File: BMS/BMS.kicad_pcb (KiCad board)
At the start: 4 copper layers, 151.1 x 100 mm, 323 parts, among them IC1 STM32H742VIT6, IC2 TPS563200DDCR, J1 Conn_01x17, J10 Conn_01x06, J11 Conn_01x06, J12 Conn_01x17, J13 USB_A, J14 USB_C_Receptacle_USB2.0_14P, J15 Harwin M80-8542042, J16 Harwin M80-8542042, J17 Conn_01x04, J18 Conn_01x02, J7 FTSH-107-01-L-D-K, J8 Conn_01x02, J9 Conn_01x06, Q1 NPN, Q2 NPN, Q3 DMT6018LDR-7, Q4 DMT6018LDR-7, Q5 DMT6018LDR-7, Q6 DMT6018LDR-7, SW1 SW_Push, U1 BQ79614PAPRQ1, U2 BQ79614PAPRQ1, U3 PBQ79600PWQ1, U4 MCP2542FD-E/MF, U5 PTPSM863253RDXR

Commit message: zmiany w bq79614 layout
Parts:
- added TH1: 10k b= 3000, Resistor_SMD:R_0603_1608Metric_Pad0.98x0.95mm_HandSolder, F.Cu at (112.2, 55.6)
- J16: value Harwin M80-8542042 -> Conn_01x10; footprint footrpint:HARWIN_M80-8542042 -> footrpint:HARWIN_G125-MV11005L1P
- moved C59 249.7 mm to (140.6, 73.2), turned to -90 degrees
- moved C60 248.2 mm to (145.7, 73.2), turned to -90 degrees
- moved C62 247.5 mm to (144.2, 69.9), turned to -90 degrees
- moved C61 245.1 mm to (142.1, 69.9), turned to -90 degrees
- moved R67 242.1 mm to (143.2, 75.7)
- moved R68 241.5 mm to (142.1, 73.2), turned to 90 degrees
- moved R71 99.9 mm to (144.2, 73.2), turned to 90 degrees
- moved J18 81.3 mm to (200.1, -20.4)
- moved R165 81.3 mm to (194.9, -24.5)
- moved U5 81.3 mm to (189.9, -12.2)
- moved C119 81.3 mm to (181.3, -22.4)
- moved C120 81.3 mm to (178.6, -22.6)
- moved C121 81.3 mm to (190.7, -24.8)
- moved C122 81.3 mm to (177.2, -25.2)
- moved C123 81.3 mm to (177.2, -27.4)
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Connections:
- C9 pad 1: Net-(U1-AVSS) -> Stack-
- J1 pad 1: Stack- -> unconnected-(J1-Pin_1-Pad1)
- J1 pad 14: Batt_Coupling -> Net-(J1-Pin_14)
- J1 pad 15: unconnected-(J1-Pin_15-Pad15) -> Net-(J1-Pin_15)
- J1 pad 16: unconnected-(J1-Pin_16-Pad16) -> Net-(J1-Pin_16)
- J1 pad 17: unconnected-(J1-Pin_17-Pad17) -> Batt_Coupling
- J1 pad 2: Net-(J1-Pin_2) -> unconnected-(J1-Pin_2-Pad2)
- J1 pad 3: Net-(J1-Pin_3) -> unconnected-(J1-Pin_3-Pad3)
- J1 pad 4: Net-(J1-Pin_4) -> Stack-
- J16 pad 1: Stack- -> /Mesurements_LTC1/Temperature_LTC_1/Thermistor2
- J16 pad 10: unconnected-(J16-Pad10) -> /Mesurements_LTC1/Temperature_LTC_1/Thermistor7
- J16 pad 2: Stack- -> /Mesurements_LTC1/Temperature_LTC_1/Thermistor3
- J16 pad 3: Stack- -> /Mesurements_LTC1/Temperature_LTC_1/Thermistor4
- J16 pad 4: Stack- -> /Mesurements_LTC1/Temperature_LTC_1/Thermistor5
- J16 pad 5: Stack- -> /Mesurements_LTC1/Temperature_LTC_1/Thermistor6
- J16 pad 9: unconnected-(J16-Pad9) -> /Mesurements_LTC1/Temperature_LTC_1/Thermistor8
- R14 pad 2: /Mesurements_LTC1/Temperature_LTC_1/Thermistor1 -> Net-(R14-Pad2)
- R15 pad 1: /Mesurements_LTC1/Temperature_LTC_1/Thermistor1 -> Net-(R14-Pad2)
- R21 pad 1: Net-(J1-Pin_13) -> Net-(J1-Pin_16)
- R22 pad 1: Net-(J1-Pin_12) -> Net-(J1-Pin_15)
- R23 pad 1: Net-(J1-Pin_11) -> Net-(J1-Pin_14)
- R24 pad 1: Net-(J1-Pin_10) -> Net-(J1-Pin_13)
- R25 pad 1: Net-(J1-Pin_9) -> Net-(J1-Pin_12)
- R26 pad 1: Net-(J1-Pin_8) -> Net-(J1-Pin_11)
- R27 pad 1: Net-(J1-Pin_7) -> Net-(J1-Pin_10)
- R28 pad 1: Net-(J1-Pin_6) -> Net-(J1-Pin_9)
- R29 pad 1: Net-(J1-Pin_5) -> Net-(J1-Pin_8)
- R30 pad 1: Net-(J1-Pin_4) -> Net-(J1-Pin_7)
- R31 pad 1: Net-(J1-Pin_3) -> Net-(J1-Pin_6)
- R32 pad 1: Net-(J1-Pin_2) -> Net-(J1-Pin_5)
- R34 pad 1: Net-(J1-Pin_13) -> Net-(J1-Pin_16)
- R35 pad 1: Net-(J1-Pin_12) -> Net-(J1-Pin_15)
- R36 pad 1: Net-(J1-Pin_11) -> Net-(J1-Pin_14)
- R37 pad 1: Net-(J1-Pin_10) -> Net-(J1-Pin_13)
- R38 pad 1: Net-(J1-Pin_9) -> Net-(J1-Pin_12)
- R39 pad 1: Net-(J1-Pin_8) -> Net-(J1-Pin_11)
- R40 pad 1: Net-(J1-Pin_7) -> Net-(J1-Pin_10)
- R41 pad 1: Net-(J1-Pin_6) -> Net-(J1-Pin_9)
- R42 pad 1: Net-(J1-Pin_5) -> Net-(J1-Pin_8)
- R43 pad 1: Net-(J1-Pin_4) -> Net-(J1-Pin_7)
- R44 pad 1: Net-(J1-Pin_3) -> Net-(J1-Pin_6)
- R45 pad 1: Net-(J1-Pin_2) -> Net-(J1-Pin_5)
- R8 pad 2: /Mesurements_LTC1/Temperature_LTC_1/Thermistor1 -> Net-(R14-Pad2)
- U1 pad 39: Net-(U1-AVSS) -> Stack-
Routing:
- net Stack-: track 7.50 -> 99.6 mm, vias 0 -> 68
- net Net-(J1-Pin_13): track 96.3 -> 26.5 mm, vias 1 -> 0
- net Net-(J1-Pin_12): track 92.9 -> 29.0 mm, vias 1 -> 0
- net Net-(J1-Pin_11): track 87.9 -> 31.9 mm, vias 1 -> 0
- net Net-(J1-Pin_10): track 83.7 -> 34.6 mm, vias 1 -> 0
- net /Mesurements_LTC1/VC7: track 84.7 -> 39.8 mm
- net Net-(J1-Pin_9): track 76.7 -> 38.0 mm, vias 1 -> 0
- net /Mesurements_LTC1/CB13: track 27.5 -> 58.4 mm, vias 0 -> 2
- net /Mesurements_LTC1/CB0: track 19.2 -> 49.8 mm, vias 0 -> 2
- net Net-(J1-Pin_5): track 19.7 -> 48.4 mm, vias 1 -> 0
- net /Mesurements_LTC1/CB1: track 17.5 -> 44.0 mm, vias 0 -> 2
- net /Mesurements_LTC1/CB2: track 15.7 -> 40.7 mm, vias 0 -> 2
- net /Mesurements_LTC1/CB12: track 31.3 -> 55.9 mm, vias 0 -> 2
- net Net-(J1-Pin_6): track 22.2 -> 45.7 mm, vias 1 -> 0
- net Net-(J1-Pin_14): track 0.00 -> 23.0 mm
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- added copper zone on F.Cu, net Stack-
- added copper zone on In1.Cu, net Stack-
- added copper zone on In2.Cu, net Stack-
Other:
- board size 151.1 x 100 mm -> 129.9 x 93.1 mm

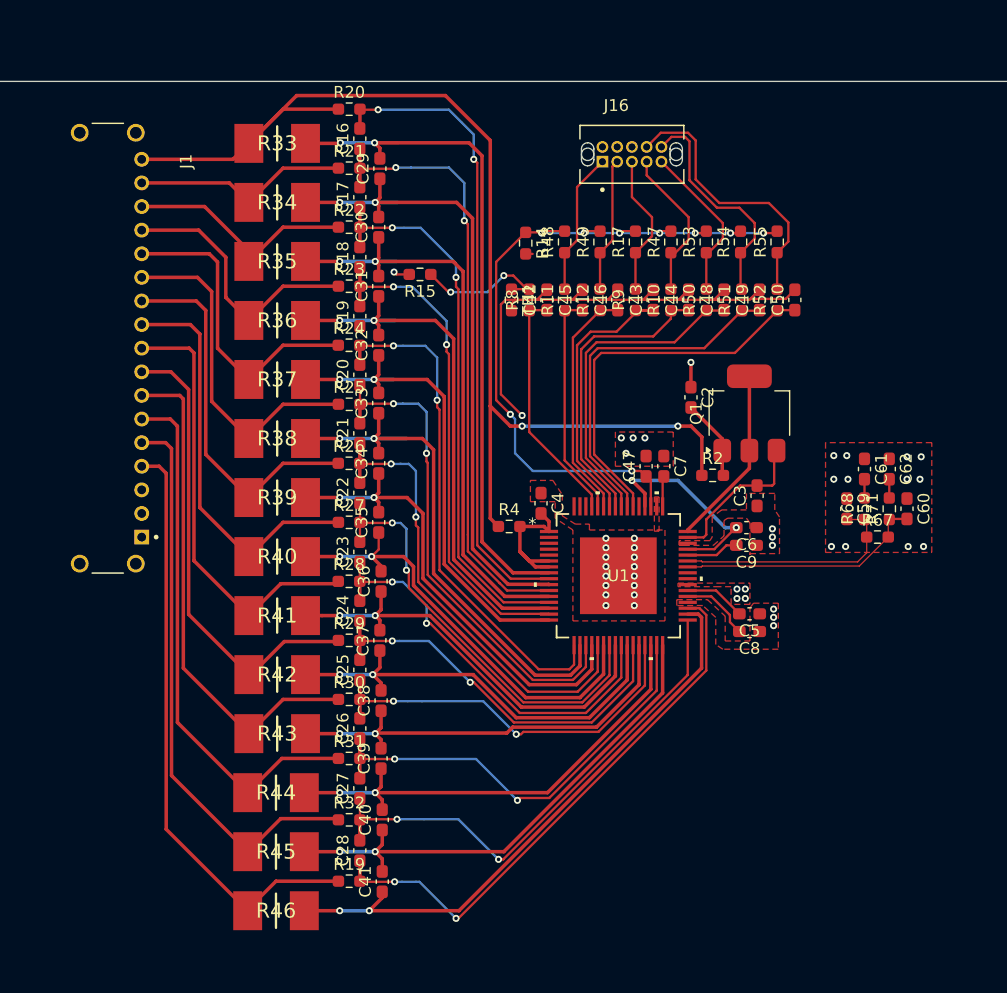
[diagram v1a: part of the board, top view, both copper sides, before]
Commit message: zmiana polozenia zlacza oraz ukladu bq, jak i zmiena via na thru
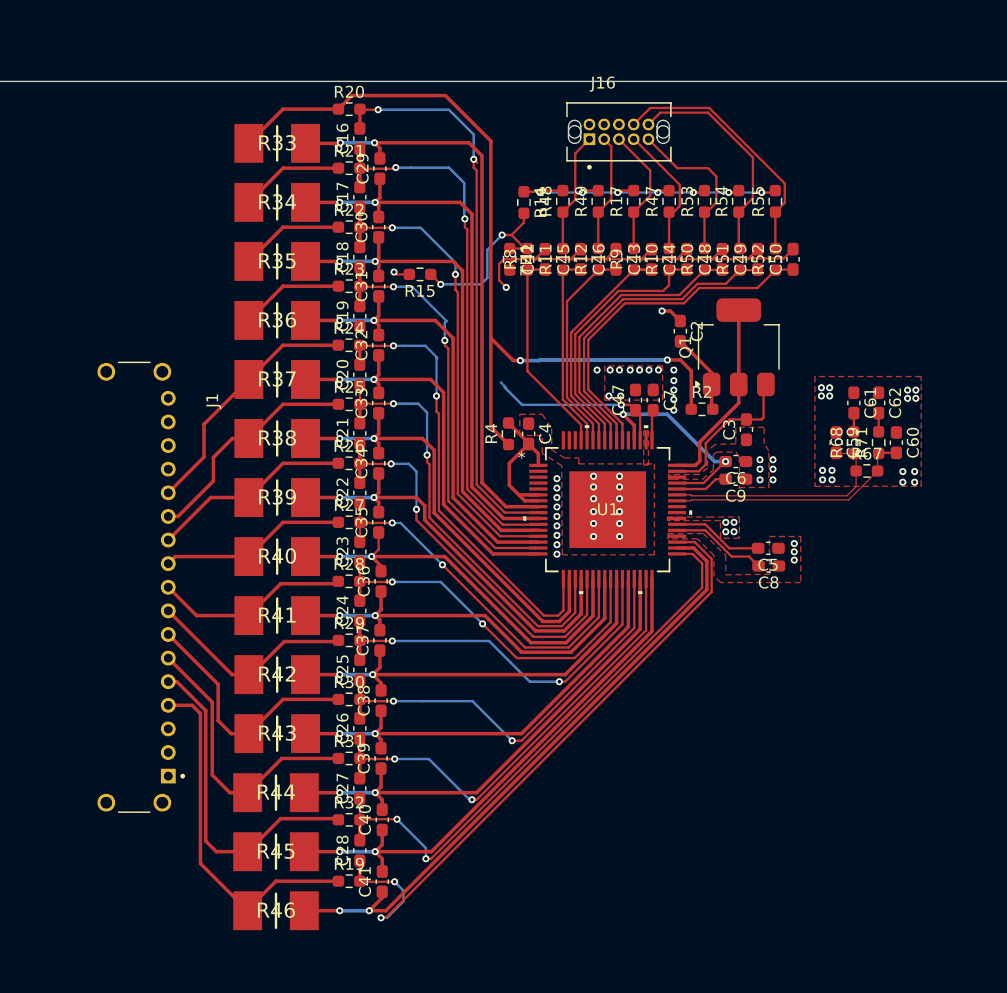
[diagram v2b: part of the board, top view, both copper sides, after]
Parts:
- moved J1 20.4 mm to (80.2, 79.9)
- moved R4 7.85 mm to (111.9, 66.9), turned to 90 degrees
- moved C4 5.98 mm to (113.6, 66.9)
- moved C8 5.78 mm to (133.9, 78.1)
- moved C5 5.77 mm to (133.9, 76.6)
- moved C61 5.67 mm to (141.2, 64.3)
- moved C62 5.67 mm to (143.2, 64.3)
- moved R2 5.67 mm to (128.3, 64.8)
- moved R67 5.67 mm to (142.2, 70.0)
- moved C47 5.67 mm to (122.7, 64.0)
- moved C7 5.67 mm to (124.2, 64.0)
- moved U1 5.67 mm to (120.3, 73.3)
- moved C3 5.67 mm to (132.1, 66.5)
- moved Q1 5.67 mm to (131.4, 59.6)
- moved C2 5.67 mm to (126.5, 58.2)
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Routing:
- net Stack-: track 99.6 -> 70.6 mm, vias 68 -> 67
- net Batt_Coupling: track 97.4 -> 71.5 mm
- net Net-(J1-Pin_7): track 43.1 -> 20.9 mm
- net Net-(J1-Pin_8): track 39.6 -> 17.9 mm
- net Net-(J1-Pin_6): track 45.7 -> 24.0 mm
- net Net-(J1-Pin_9): track 38.0 -> 17.0 mm
- net Net-(J1-Pin_5): track 48.4 -> 28.1 mm
- net /Mesurements_LTC1/Temperature_LTC_1/TSREF: track 64.2 -> 44.4 mm, vias 9 -> 8
- net Net-(J1-Pin_10): track 34.6 -> 16.1 mm
- net Net-(J1-Pin_11): track 31.9 -> 17.1 mm
- net Net-(J1-Pin_14): track 23.0 -> 8.79 mm
- net Net-(J1-Pin_15): track 20.4 -> 8.86 mm
- net Net-(J1-Pin_16): track 18.5 -> 8.79 mm
- net Net-(J1-Pin_12): track 29.0 -> 19.5 mm
- net /Mesurements_LTC1/CB13: track 58.4 -> 50.3 mm
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
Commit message: Dodano layout drugiego bq79614, ukladu tlumaczącego z protokułu TI na UART oraz wstępnie poprowadzono pary różnicowe
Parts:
- removed F2: 1 ALBO 2 A, Resistor_SMD:R_0402_1005Metric_Pad0.72x0.64mm_HandSolder
- removed J11, J9: Conn_01x06, footrpint:HARWIN_M300-MV30645M1
- removed J15: Harwin M80-8542042, footrpint:HARWIN_M80-8542042
- removed J17: Conn_01x04, footrpint:HARWIN_M80-5100442
- removed J18: Conn_01x02, footrpint:HARWIN_M80-5000000M1-02-PM1-00-000
- removed J5, J6: ~, footrpint:HARWIN_M80-5000000M1-02-PM1-00-000
- removed J8: Conn_01x02, footrpint:HARWIN_M55-3100242R
- removed Q5: DMT6018LDR-7, Samacsys:DMT6018LDR7
- removed R162: 100, Resistor_SMD:R_0603_1608Metric
- removed R164: 4.7k, Resistor_SMD:R_0603_1608Metric
- added J19: Conn_02x13_Counter_Clockwise, footrpint:HARWIN_M80-5402642, F.Cu at (-16.5, 173.1)
- added TH13: 10k b= 3000, Resistor_SMD:R_0603_1608Metric_Pad0.98x0.95mm_HandSolder, F.Cu at (111.5, 127.5)
- J10: value Conn_01x06 -> Conn_01x10; footprint footrpint:HARWIN_M300-MV30645M1 -> footrpint:HARWIN_G125-MV11005L1P
- moved J10 259.2 mm to (121.5, 117.6)
- moved C64 259.0 mm to (149.2, 164.1), turned to -90 degrees
- moved C63 254.9 mm to (144.3, 164.1), turned to -90 degrees
- moved R74 251.2 mm to (146.8, 166.5)
- moved R73 250.3 mm to (145.8, 164.1), turned to -90 degrees
- moved C54 245.9 mm to (133.8, 151.2), turned to 180 degrees
- moved C57 244.7 mm to (133.8, 152.8), turned to 180 degrees
- moved C52 243.4 mm to (132.4, 141.0), turned to 90 degrees
- moved C55 241.4 mm to (131.2, 144.3), turned to 180 degrees
- moved C58 240.4 mm to (131.2, 145.8), turned to 180 degrees
- moved U3 235.5 mm to (148.0, 175.2), turned to 180 degrees
- moved C51 234.5 mm to (124.1, 134.4), turned to 90 degrees
- moved C56 233.0 mm to (124.1, 138.0), turned to -90 degrees
- moved R64 228.6 mm to (126.7, 140.0)
- moved C53 224.7 mm to (113.6, 142.0), turned to -90 degrees
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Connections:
- net Net-(C12-Pad1) renamed /galvanic_isulation_2/S2+
- net Net-(C12-Pad2) renamed /galvanic_isulation_2/S1+
- net Net-(C13-Pad1) renamed /galvanic_isulation_2/S2-
- net Net-(C13-Pad2) renamed /galvanic_isulation_2/S1-
- net Net-(C130-Pad1) renamed /galvanic_isulation_1/S2+
- net Net-(C130-Pad2) renamed /galvanic_isulation_1/S1+
- net Net-(C131-Pad1) renamed /galvanic_isulation_1/S2-
- net Net-(C131-Pad2) renamed /galvanic_isulation_1/S1-
- net Net-(C61-Pad1) renamed /galvanic_isulation_0/S2+
- net Net-(C61-Pad2) renamed /galvanic_isulation_0/S1+
- net Net-(C62-Pad1) renamed /galvanic_isulation_0/S2-
- net Net-(C62-Pad2) renamed /galvanic_isulation_0/S1-
- net Net-(D1-A) renamed /Connectivity/Relay_OUT
- net Net-(D13-A) renamed /Connectivity/PreCharge_OUT
- C115 pad 2: +5V -> /Connectivity/+5V_curr_sense
- C122 pad 1: /Power/5V/+5V_OUT -> +5V
- C123 pad 1: /Power/5V/+5V_OUT -> +5V
- C126 pad 1: /Power/5V/+5V_OUT -> +5V
- C127 pad 1: /Power/5V/+5V_OUT -> +5V
- D6 pad 1: +5V -> /Connectivity/+5V_curr_sense
- D8 pad 2: Net-(D8-A) -> VBUS
- F1 pad 2: /Connectivity/Ext_5V -> /Connectivity/5V_fused
- IC1 pad 30: /3.3V_Enable -> unconnected-(IC1-PA6-Pad30)
- J10 pad 1: /Connectivity/Ext_3.3V -> /Mesurements_LTC2/Temperature_LTC_2/Thermistor2
- J10 pad 2: Net-(J10-Pin_2) -> /Mesurements_LTC2/Temperature_LTC_2/Thermistor3
- J10 pad 3: /Connectivity/Ext_3.3V -> /Mesurements_LTC2/Temperature_LTC_2/Thermistor4
- J10 pad 4: Net-(J10-Pin_2) -> /Mesurements_LTC2/Temperature_LTC_2/Thermistor5
- J10 pad 5: /Connectivity/Ext_3.3V -> /Mesurements_LTC2/Temperature_LTC_2/Thermistor6
- J10 pad 6: Net-(J10-Pin_2) -> Batt_Coupling
- J13 pad 1: Net-(J13-VBUS) -> VBUS
- L1 pad 2: /Power/5V/+5V_OUT -> +5V
- Q4 pad 6: Net-(J9-Pin_2) -> /Connectivity/5V_fused_minus
- R149 pad 1: /Connectivity/B1_IN -> /Connectivity/B2_IN
- R156 pad 1: /Connectivity/B2_IN -> /Connectivity/B3_IN
- R158 pad 1: /Connectivity/B3_IN -> /Connectivity/B4_IN
- R165 pad 2: /Power/5V/+5V_OUT -> +5V
- R61 pad 1: /Power/5V/+5V_OUT -> +5V
- U5 pad 1: /Power/5V/+5V_OUT -> +5V
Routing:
- net Batt_Coupling: track 71.5 -> 270.6 mm, vias 2 -> 78
- net CELL26: track 0.00 -> 81.0 mm, vias 0 -> 2
- net +5V: track 0.00 -> 60.5 mm
- net /Power/5V/+5V_OUT: track 60.5 -> 0.00 mm
- net /galvanic_isulation_0/S2-: track 0.00 -> 53.5 mm, vias 0 -> 2
- net /Mesurements_LTC2/CB0: track 0.00 -> 52.8 mm, vias 0 -> 2
- net /galvanic_isulation_0/S2+: track 0.00 -> 52.6 mm
- net /Mesurements_LTC2/CB13: track 0.00 -> 50.2 mm, vias 0 -> 2
- net /Mesurements_LTC2/VC0: track 0.00 -> 49.7 mm, vias 0 -> 2
- net /Mesurements_LTC2/VC1: track 0.00 -> 48.2 mm, vias 0 -> 2
- net /Mesurements_LTC2/CB12: track 0.00 -> 47.8 mm, vias 0 -> 2
- net /Mesurements_LTC2/VC13: track 0.00 -> 46.6 mm, vias 0 -> 2
- net /galvanic_isulation_0/S1+: track 1.59 -> 47.5 mm
- net /Mesurements_LTC2/CB1: track 0.00 -> 45.6 mm, vias 0 -> 2
- net /galvanic_isulation_0/S1-: track 1.59 -> 46.7 mm
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- added copper zone on F.Cu, net Batt_Coupling
- added copper zone on In1.Cu, net Batt_Coupling
- added copper zone on In2.Cu, net Batt_Coupling
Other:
- board size 129.9 x 93.1 mm -> 119.4 x 147.2 mm

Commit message: Iteracja 1.0 gotowa, teraz sprawdzenie i zmiany kosmetyczne
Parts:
- removed J14: USB_C_Receptacle_USB2.0_14P, Connector_USB:USB_C_Receptacle_GCT_USB4110
- removed Q3, Q4, Q6: DMT6018LDR-7, Samacsys:DMT6018LDR7
- added C134: 1uF, Capacitor_SMD:C_0603_1608Metric_Pad1.08x0.95mm_HandSolder, F.Cu at (177.2, 90.3)
- added C135: 1uF, Capacitor_SMD:C_0603_1608Metric_Pad1.08x0.95mm_HandSolder, F.Cu at (177.2, 91.8)
- added C136: 1uF, Capacitor_SMD:C_0603_1608Metric_Pad1.08x0.95mm_HandSolder, F.Cu at (167.3, 114.3)
- added C137: 1uF, Capacitor_SMD:C_0603_1608Metric_Pad1.08x0.95mm_HandSolder, F.Cu at (173.6, 88.3)
- added C138: 1uF, Capacitor_SMD:C_0603_1608Metric_Pad1.08x0.95mm_HandSolder, F.Cu at (172.1, 88.3)
- added C65: 1uF, Capacitor_SMD:C_0603_1608Metric_Pad1.08x0.95mm_HandSolder, F.Cu at (157.1, 147.5)
- added C66: 1uF, Capacitor_SMD:C_0603_1608Metric_Pad1.08x0.95mm_HandSolder, F.Cu at (162.8, 140.6)
- added C67: 1uF, Capacitor_SMD:C_0603_1608Metric_Pad1.08x0.95mm_HandSolder, F.Cu at (176.4, 140.4)
- added C68: 1uF, Capacitor_SMD:C_0603_1608Metric_Pad1.08x0.95mm_HandSolder, F.Cu at (160.8, 159.7)
- added C69: 1uF, Capacitor_SMD:C_0603_1608Metric_Pad1.08x0.95mm_HandSolder, F.Cu at (177.2, 158.7)
- added C70: 1uF, Capacitor_SMD:C_0603_1608Metric_Pad1.08x0.95mm_HandSolder, F.Cu at (170.9, 113.5)
- added F2: 3A, Fuse:Fuse_0603_1608Metric_Pad1.05x0.95mm_HandSolder, F.Cu at (172.9, 91.9)
- added J11: USB4235-03-C_REVA, footrpint:GCT_USB4235-03-C_REVA, F.Cu at (183.7, 151.0)
- added JP1: Jumper_2_Small_Open, Jumper:SolderJumper-2_P1.3mm_Open_Pad1.0x1.5mm, F.Cu at (176.2, 137.8)
- added Q5: DMT6018LDR-7, Samacsys:DMT6018LDR7, F.Cu at (157.5, 120.4)
- added Q7: DMT6018LDR-7, Samacsys:DMT6018LDR7, F.Cu at (178.8, 110.7)
- added R75: 5.1K, Resistor_SMD:R_0603_1608Metric, F.Cu at (181.0, 154.9)
- added R76: 5.1K, Resistor_SMD:R_0603_1608Metric, F.Cu at (184.0, 144.4)
- added REF**: MountingHole_3.2mm_M3_Pad_Via, MountingHole:MountingHole_3.2mm_M3_Pad_Via, F.Cu at (146.9, 180.9)
- added REF**: MountingHole_3.2mm_M3_Pad_Via, MountingHole:MountingHole_3.2mm_M3_Pad_Via, F.Cu at (82.9, 41.9)
- added REF**: MountingHole_3.2mm_M3_Pad_Via, MountingHole:MountingHole_3.2mm_M3_Pad_Via, F.Cu at (83.9, 180.9)
- added REF**: MountingHole_3.2mm_M3_Pad_Via, MountingHole:MountingHole_3.2mm_M3_Pad_Via, F.Cu at (181.9, 85.4)
- added REF**: MountingHole_3.2mm_M3_Pad_Via, MountingHole:MountingHole_3.2mm_M3_Pad_Via, F.Cu at (145.9, 42.9)
- added TP1: TestPoint_Small, TestPoint:TestPoint_Pad_D1.0mm, B.Cu at (174.4, 106.2)
- added TP10: TestPoint_Small, TestPoint:TestPoint_Pad_D1.0mm, B.Cu at (171.5, 122.5)
- added TP11: TestPoint_Small, TestPoint:TestPoint_Pad_D1.0mm, B.Cu at (170.2, 117.9)
- added TP12: TestPoint_Small, TestPoint:TestPoint_Pad_D1.0mm, B.Cu at (177.3, 98.3)
- added TP13: TestPoint_Small, TestPoint:TestPoint_Pad_D1.0mm, B.Cu at (179.9, 93.8)
- added TP14: TestPoint_Small, TestPoint:TestPoint_Pad_D1.0mm, B.Cu at (175.6, 120.5)
- added TP15: TestPoint_Small, TestPoint:TestPoint_Pad_D1.0mm, B.Cu at (164.3, 87.5)
- added TP16: TestPoint_Small, TestPoint:TestPoint_Pad_D1.0mm, B.Cu at (172.9, 95.3)
- added TP17: TestPoint_Small, TestPoint:TestPoint_Pad_D1.0mm, B.Cu at (178.7, 118.8)
- added TP18: TestPoint_Small, TestPoint:TestPoint_Pad_D1.0mm, B.Cu at (177.1, 101.3)
- added TP2: TestPoint_Small, TestPoint:TestPoint_Pad_D1.0mm, B.Cu at (166.2, 122.5)
- added TP3: TestPoint_Small, TestPoint:TestPoint_Pad_D1.0mm, B.Cu at (154.3, 116.9)
- added TP4: TestPoint_Small, TestPoint:TestPoint_Pad_D1.0mm, B.Cu at (179.8, 104.5)
- added TP5: TestPoint_Small, TestPoint:TestPoint_Pad_D1.0mm, B.Cu at (168.5, 123.8)
- added TP6: TestPoint_Small, TestPoint:TestPoint_Pad_D1.0mm, B.Cu at (174.9, 162.6)
- added TP7: TestPoint_Small, TestPoint:TestPoint_Pad_D1.0mm, B.Cu at (164.5, 168.8)
- added TP8: TestPoint_Small, TestPoint:TestPoint_Pad_D1.0mm, B.Cu at (161.7, 166.7)
- added TP9: TestPoint_Small, TestPoint:TestPoint_Pad_D1.0mm, B.Cu at (169.3, 126.9)
- C110, C111, C112, C114, C115, C116, C117, C118: footprint Capacitor_SMD:C_0603_1608Metric -> Capacitor_SMD:C_0603_1608Metric_Pad1.08x0.95mm_HandSolder
- C141: value 47n -> 47n
- F1: value 1 ALBO 2 A -> 3A; footprint Resistor_SMD:R_0402_1005Metric_Pad0.72x0.64mm_HandSolder -> Fuse:Fuse_0603_1608Metric_Pad1.05x0.95mm_HandSolder
- F3: value 4A -> 3A; footprint Resistor_SMD:R_0402_1005Metric_Pad0.72x0.64mm_HandSolder -> Fuse:Fuse_0603_1608Metric_Pad1.05x0.95mm_HandSolder
- R151, R152, R153, R154, R160, R161, R163: footprint Resistor_SMD:R_0603_1608Metric -> Resistor_SMD:R_0603_1608Metric_Pad0.98x0.95mm_HandSolder
- R64: value 300 -> 300
- moved C116 323.5 mm to (176.6, 132.9), turned to 90 degrees
- moved C111 318.9 mm to (169.8, 163.9), turned to -90 degrees
- moved R163 318.2 mm to (178.9, 113.5), turned to 180 degrees
- moved R161 315.2 mm to (176.0, 111.2), turned to -90 degrees
- moved C117 314.5 mm to (171.5, 132.9), turned to 90 degrees
- moved C112 314.1 mm to (165.2, 163.9), turned to -90 degrees
- moved C115 313.6 mm to (166.7, 136.9), turned to 90 degrees
- moved C110 313.4 mm to (166.4, 127.7), turned to 90 degrees
- moved C118 312.7 mm to (169.7, 135.5)
- moved R160 311.6 mm to (172.4, 138.0), turned to 90 degrees
- moved F1 310.9 mm to (179.4, 116.0)
- moved C114 309.4 mm to (160.8, 163.9), turned to -90 degrees
- moved R154 305.7 mm to (162.8, 137.4), turned to 90 degrees
- moved J7 303.9 mm to (182.9, 136.4), turned to -90 degrees
- moved R153 303.2 mm to (160.3, 137.4), turned to 90 degrees
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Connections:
- net /CAN_RX renamed /CAN_OUT-
- net /CAN_TX renamed /CAN_OUT+
- net /Connectivity/LED4 renamed Net-(D2-K)
- net Net-(D12-K-Pad1) renamed /Connectivity/NP
- net Net-(D12-K-Pad3) renamed /Connectivity/DP
- net Net-(Q4B-G2) renamed /Connectivity/G3
- D1 pad 2: /Connectivity/Relay_OUT -> /Connectivity/D1
- D13 pad 2: /Connectivity/PreCharge_OUT -> /Connectivity/D2
- D3 pad 1: /LED3 -> Net-(D3-K)
- D4 pad 1: /LED2 -> Net-(D4-K)
- D5 pad 1: /LED1 -> Net-(D5-K)
- D6 pad 3: /Curr_sense -> /Curr_sense2
- J19 pad 10: /Connectivity/5V_fused_minus -> /Connectivity/5V_fused
- J19 pad 11: GND -> unconnected-(J19-Pin_11-Pad11)
- J19 pad 17: /Connectivity/5V_fused -> GND
- J19 pad 18: /Connectivity/5V_fused -> /Connectivity/Curr_sense_out
- J19 pad 19: +12V -> /Curr_sense2
- J19 pad 2: /Connectivity/B2_IN -> /Connectivity/+5V_curr_sense
- J19 pad 20: +12V -> GND
- J19 pad 21: /Curr_sense2 -> GND
- J19 pad 22: GND -> /Connectivity/B4_IN
- J19 pad 24: GND -> /Connectivity/B3_IN
- J19 pad 26: GND -> /Connectivity/B2_IN
- J19 pad 3: /Connectivity/B3_IN -> +12V
- J19 pad 4: /Connectivity/B4_IN -> +12V
- J19 pad 5: /Connectivity/+5V_curr_sense -> /Connectivity/D2
- J19 pad 6: /Curr_sense -> /Connectivity/D1
- J19 pad 7: /Connectivity/Relay_OUT -> /Connectivity/5V_fused_minus
- J19 pad 8: /Connectivity/PreCharge_OUT -> /Connectivity/5V_fused_minus
- J19 pad 9: /Connectivity/5V_fused_minus -> /Connectivity/5V_fused
- R152 pad 2: /LED3 -> Net-(D3-K)
- R153 pad 2: /LED2 -> Net-(D4-K)
- R154 pad 2: /LED1 -> Net-(D5-K)
- R160 pad 1: /Curr_sense -> /Connectivity/Curr_sense_out
- R173 pad 1: /USB2- -> /USB2+
- R174 pad 1: /USB2+ -> /USB2-
- R3 pad 2: /Connectivity/Relays/G2 -> /Connectivity/G1
- R56 pad 2: /Connectivity/Relays/G2 -> /Connectivity/G1
- R58 pad 2: /Connectivity/Relays/G2 -> /Connectivity/G2
- R59 pad 2: /Connectivity/Relays/G2 -> /Connectivity/G2
- U5 pad 3: +3.3V -> Net-(U5-FB)
- U5 pad 7: +3.3V -> Net-(U5-FB)
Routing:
- net +3.3V: track 30.7 -> 246.3 mm, vias 4 -> 16
- net +12V: track 1.53 -> 152.7 mm, vias 0 -> 4
- net /Curr_sense2: track 0.00 -> 93.9 mm, vias 0 -> 3
- net /Button1: track 0.00 -> 71.3 mm, vias 0 -> 4
- net /Connectivity/B4_IN: track 0.00 -> 64.5 mm, vias 0 -> 1
- net /Connectivity/B3_IN: track 0.00 -> 59.0 mm, vias 0 -> 1
- net /NRST: track 0.00 -> 58.8 mm, vias 0 -> 2
- net /Curr_sense: track 0.00 -> 56.8 mm, vias 0 -> 4
- net /Connectivity/B2_IN: track 0.00 -> 56.2 mm, vias 0 -> 1
- net /Connectivity/Curr_sense_out: track 0.00 -> 51.5 mm, vias 0 -> 5
- net /SIGNAL_PRECHARGE: track 0.00 -> 51.1 mm, vias 0 -> 3
- net /SIGNAL_RELAY: track 0.00 -> 51.0 mm, vias 0 -> 3
- net /Connectivity/+5V_curr_sense: track 0.00 -> 45.6 mm, vias 0 -> 1
- net /Connectivity/D2: track 0.00 -> 40.9 mm, vias 0 -> 1
- net /Connectivity/D1: track 0.00 -> 39.1 mm, vias 0 -> 1
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- added copper zone on F.Cu, net /Connectivity/5V_fused
- added copper zone on F.Cu, net /Connectivity/5V_fused_minus
- added copper zone on B.Cu, net GND
- added copper zone on In1.Cu, net GND
- added copper zone on In2.Cu, net GND
- removed copper zone on F.Cu, net +12V
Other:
- board size 119.4 x 147.2 mm -> 111 x 147 mm
- board text added: "Battery Management System"
- board text added: "Dsigned by : Wiktor Krakowski"
- board text added: "HV"

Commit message: poprawy
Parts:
- removed REF** (x5): MountingHole_3.2mm_M3_Pad_Via, MountingHole:MountingHole_3.2mm_M3_Pad_Via
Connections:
- C10 pad 1: Batt_Coupling -> GND
- C11 pad 1: Batt_Coupling -> GND
- C14 pad 1: GND -> Batt_Coupling
- C15 pad 1: GND -> Batt_Coupling
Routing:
- net VBUS: track 0.00 -> 129.8 mm, vias 0 -> 2
- net /12V_Enable: track 6.47 -> 87.5 mm, vias 1 -> 2
- net +5V: track 87.4 -> 109.1 mm
- net /Mesurements_LTC2/Temperature_LTC_2/TSREF: track 36.5 -> 57.6 mm, vias 7 -> 8
- net Batt_Coupling: track 270.6 -> 279.8 mm, vias 62 -> 84
- net Net-(Q2-E): track 3.06 -> 12.1 mm
- net /NRST: track 58.8 -> 67.0 mm
- net /STM Comunication Interface /COMHP: track 28.0 -> 31.9 mm
- net /STM Comunication Interface /COMHN: track 27.2 -> 31.1 mm
- net +3.3V: track 246.3 -> 248.8 mm, vias 16 -> 17
- net /Connectivity/G3: track 1.48 -> 3.26 mm
- net /Mesurements_LTC1/VC9: track 38.7 -> 40.3 mm
- net Stack-: vias 83 -> 92
